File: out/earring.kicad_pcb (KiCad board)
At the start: 4 copper layers, 30.5 x 35.8 mm, 144 parts, among them J1 USB-C, Q1 ALS-PT19, Q2 CJ2101, Q3 BSS138W, Q4 CJ2101, Q5 BSS138W, SW1 BOOTSEL, SW2 PWR, U1 RP2350A, U2 LGS4056H, U3 NCP730-3.3, U4 TPS22913, U5 USBLC6-2P6, U6 LSM6DS3TR-C, U7 W25Q16JVUXIQ, Y1 12MHz

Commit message: One-button BOOTSEL, silicon D2/D3, button TVS, high-Vth latch FET
Folds the power-button simulation's findings into the board (user decisions
2026-10-24), each re-simulated, independently reviewed and re-reviewed.

- SW1 deleted. A long hold on the power button resets the chip into BOOTSEL
  (Q8/R26/R27, R28 680k + C75 timer, D5, U8 74LVC2G14GW, Q7 strap, C76/R29 ->
  Q6 RUN kick, C77). Fires 2.2-10.3 s typical, 2.0-19.4 s at U8's leakage
  limit. On battery the same hold turns the board off on release, which is
  the hardware force-off for hung firmware. Flash is never touched.
- Hot self-start fixed: D2 BAT54SW -> BAV99W, D3 B5819WS -> 1N4007WS. Board-off
  EN is now <= 0.03 V at 85 C (afabd86 reached 2.27 V). Cost: VSYS = VBUS - 0.8 V.
- Button ESD: D6 PESD5V0S1BL at the switch pad + R30 1k. A +-8 kV strike puts
  <= 22 mA into the latch (was ~24 A) and no longer counts as a press.
- Q4 CJ2101 -> LBSS84WT1G (VGS(th) 0.8-2.0 V): the latch's hot off-state
  margin no longer depends on an unspecified threshold tempco (review F2;
  design/sim/button/leakstudy.py).
- D4 BAV70W sourced from Nexperia (the Diodes part was down to 100 in stock).
- Testbench: netlist from circuit.py, afabd86 kept as a reference patch,
  54/54 runs pass, ESD/II-limit/pull-up/click-then-hold scenarios added.
- Placement: 14 new parts via scan_spot (12 back, Q6/R29 front in SW1's
  spot); DRC 0 errors, placed but NOT routed. Schematic regenerated
  (97 nets verified). Gates 1/2/6/8 updated with both reviews.

Firmware must change with this board: GPIO21 is active high with no pull-up,
and the long-press-off must be <= 1.5 s.

Co-Authored-By: Claude Opus 5.5 <noreply@anthropic.com>
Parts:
- removed SW1: BOOTSEL, earring:KEY-SMD_4P-L4.2-W3.2-P2.20-LS4.6
- added C75: 10u, earring:C_0603_1608Metric, B.Cu at (100.8, 93.2)
- added C76: 10n, earring:C_0402_1005Metric, B.Cu at (104.5, 90.8)
- added C77: 100n, earring:C_0402_1005Metric, B.Cu at (106.0, 93.0)
- added D5: 1N4148WS, earring:D_SOD-323, B.Cu at (100.8, 90.8)
- added D6: PESD5V0S1BL, earring:D_SOD-882, B.Cu at (94.0, 88.2)
- added Q6: BSS138W, earring:SOT-323_MOSFET, F.Cu at (99.0, 89.0)
- added Q7: BSS138W, earring:SOT-323_MOSFET, B.Cu at (107.2, 95.2)
- added Q8: CJ2101, earring:SOT-323_MOSFET, B.Cu at (96.5, 93.2)
- added R26: 100k, earring:R_0402_1005Metric, B.Cu at (97.2, 91.5)
- added R27: 4.7k, earring:R_0402_1005Metric, B.Cu at (95.2, 91.5)
- added R28: 680k, earring:R_0402_1005Metric, B.Cu at (99.0, 93.8)
- added R29: 1M, earring:R_0402_1005Metric, F.Cu at (96.8, 87.2)
- added R30: 1k, earring:R_0402_1005Metric, B.Cu at (94.5, 90.0)
- added U8: 74LVC2G14, earring:SOT-363_SC-70-6, B.Cu at (103.5, 93.0)
- D2: value BAT54S -> BAV99W
- D3: value B5819WS -> 1N4007WS
- Q4: value CJ2101 -> LBSS84WT1G
- moved C27 3.34 mm to (93.2, 91.5), turned to 0 degrees
- moved C17 0.11 mm to (107.3, 101.9)
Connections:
- D4 pad 1: BTN_SENSE -> PRESS_N
- SW2 pad 2: BTN_N -> BTN_EXT
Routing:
- net VBUS: track 3.81 -> 6.24 mm

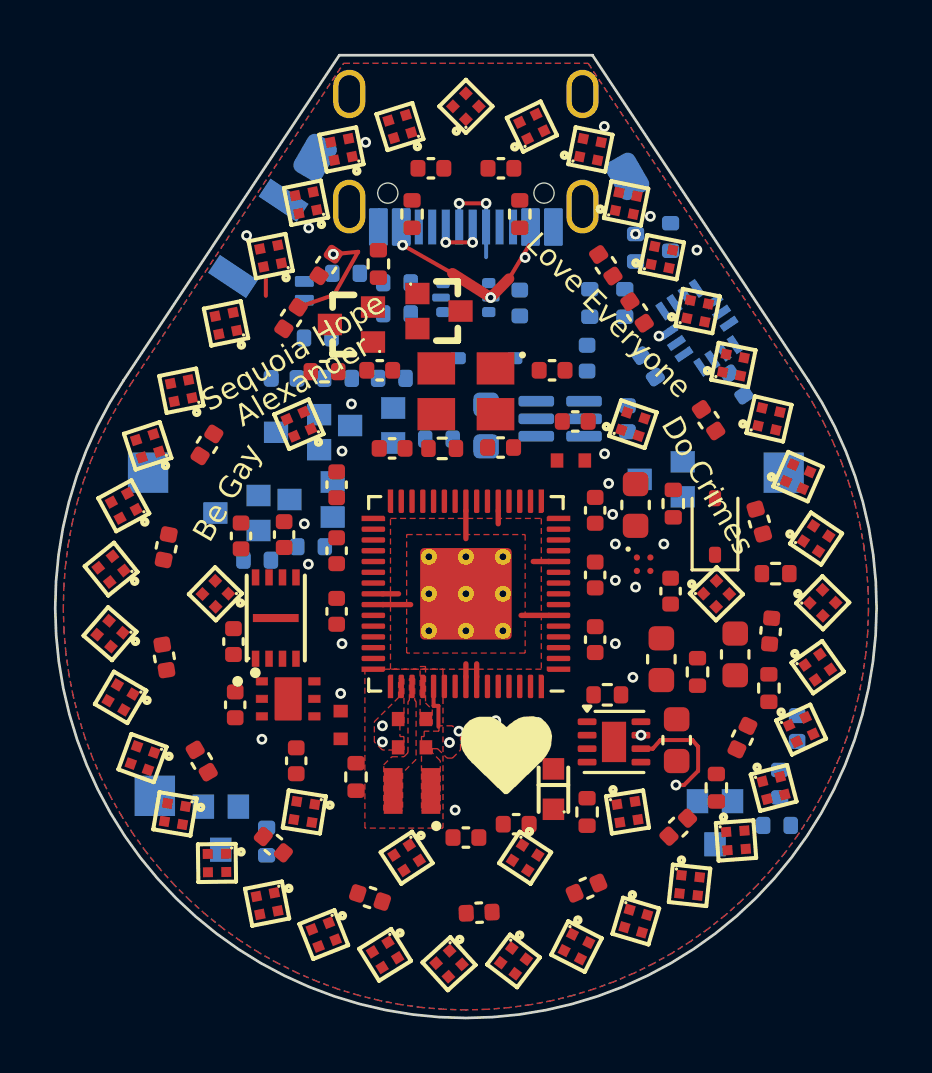
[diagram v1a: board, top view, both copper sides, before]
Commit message: LED ring: WS2816C-1313 (16-bit) in three switched zones; lock policy
User decisions 2026-10-24: switch the ring to WS2816C-1313/4P and split it
into left / right / centre zones. Independently reviewed (gates 1, 2, 6 pass).

- LEDs: SK6805-EC10 -> WS2816C-1313/4P (C42417612). 16-bit per channel plus
  gamma for the low-brightness range; VDD floor 3.3 V; idle 0.7-1.0 mA per LED;
  rated to 65 C; MSL 5a. New LED_WS2816C-1313 footprint (EasyEDA land, pin map
  checked against the datasheet: 1 VDD, 2 DO, 3 GND, 4 DI).
- Three zones, each its own chain, TPS22913 load switch (U4/U9/U10) and
  open-drain shifter pulled up to its own rail (Q3/Q9/Q10 + R23/R31/R32), so a
  dark zone draws nothing and can't be back-fed through its data line.
  Left LED1-18, right LED37->19 (reversed, enters at the tip), centre
  LED38-45. Data GPIO16/17/18 (adjacent: one PIO program), enables GPIO1/0/22.
- In2: VLED_C inner band, VLED_L / VLED_R split of the outer band, 3V3 disc.
- Placement: same ring centres, per-zone orientation; D3/C29 moved for
  LED44; zone drivers via scan_spot. DRC 0 errors, placed but NOT routed:
  the user routes it with their own GPU autorouter. route.py's SK6805-era
  freerouting workaround pre-routes are removed.
- Locked for the router: all LEDs, J1, SW2 (user request), plus BT1, Q1, and
  every part that locked copper or a fixed pour lands on (U1, U2, U5, R14,
  VREG cluster L1/C11/C12/C13/R13/C22). Everything else may be nudged.
- Schematic regenerated per zone (103 nets verified).

Firmware: three 48-bit chains (reset >= 280 us), data pins inverted and idle
high, power zones off rather than blanking them, keep a hard brightness cap.

Co-Authored-By: Claude Opus 5.5 <noreply@anthropic.com>
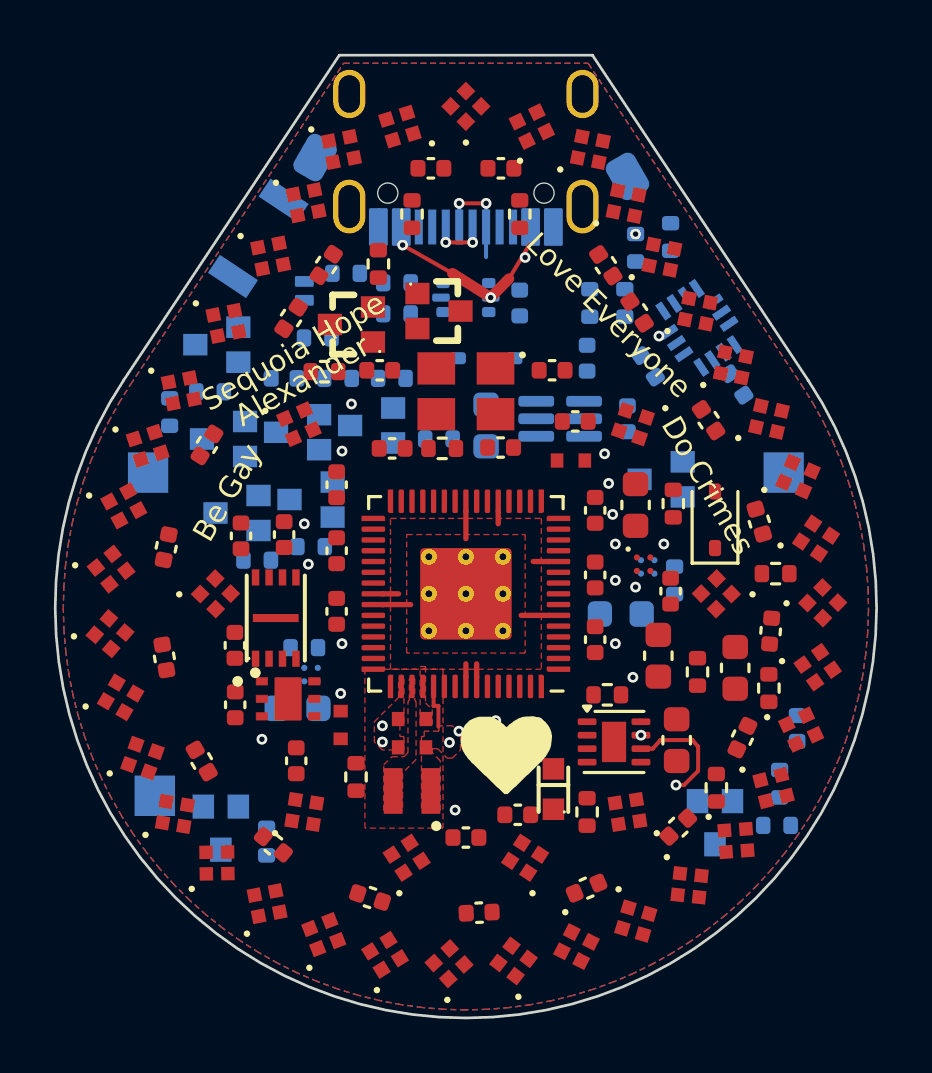
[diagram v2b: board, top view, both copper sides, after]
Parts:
- added C78: 10u, earring:C_0603_1608Metric, B.Cu at (105.8, 100.2)
- added C79: 10u, earring:C_0603_1608Metric, B.Cu at (93.8, 103.8)
- added Q10: BSS138W, earring:SOT-323_MOSFET, B.Cu at (91.0, 93.8)
- added Q9: BSS138W, earring:SOT-323_MOSFET, B.Cu at (90.8, 90.2)
- added R31: 1k, earring:R_0402_1005Metric, B.Cu at (90.5, 92.0)
- added R32: 1k, earring:R_0402_1005Metric, B.Cu at (89.0, 92.8)
- added R33: 10k, earring:R_0402_1005Metric, B.Cu at (107.8, 99.0)
- added R34: 10k, earring:R_0402_1005Metric, B.Cu at (94.0, 101.5)
- added U10: TPS22913, earring:YZV0004ADAD, B.Cu at (94.2, 102.5)
- added U9: TPS22913, earring:YZV0004ADAD, B.Cu at (106.8, 98.5)
- LED1, LED10, LED11, LED12, LED13, LED14, LED15, LED16, LED17, LED18, LED19, LED2, LED20, LED21, LED22, LED23, LED24, LED25, LED26, LED27, LED28, LED29, LED3, LED30, LED31, LED32, LED33, LED34, LED35, LED36, LED37, LED38, LED39, LED4, LED40, LED41, LED42, LED43, LED44, LED45, LED5, LED6, LED7, LED8, LED9: value SK6805-EC10 -> WS2816C-1313; footprint earring:LED_SK6805-EC10 -> earring:LED_WS2816C-1313
- moved C29 0.50 mm to (110.0, 102.2)
- moved C26 0.36 mm to (101.9, 107.7)
- moved D3 0.25 mm to (109.2, 96.8)
- moved C17 0.17 mm to (107.1, 101.8)
- moved C18 0.15 mm to (91.4, 101.4)
- turned LED1 to 11.4366 degrees
- turned LED10 to 59.6219 degrees
- turned LED11 to 70.003 degrees
- turned LED12 to 80.3842 degrees
- turned LED13 to 90.7653 degrees
- turned LED14 to 101.146 degrees
- turned LED15 to 111.528 degrees
- turned LED16 to 121.909 degrees
- turned LED17 to 132.29 degrees
- turned LED18 to 142.671 degrees
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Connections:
- net LED_D19 renamed LEDR_D18
- net LED_D20 renamed LEDR_D17
- net LED_D21 renamed LEDR_D16
- net LED_D22 renamed LEDR_D15
- net LED_D23 renamed LEDR_D14
- net LED_D24 renamed LEDR_D13
- net LED_D25 renamed LEDR_D12
- net LED_D26 renamed LEDR_D11
- net LED_D27 renamed LEDR_D10
- net LED_D28 renamed LEDR_D9
- net LED_D29 renamed LEDR_D8
- net LED_D30 renamed LEDR_D7
- net LED_D31 renamed LEDR_D6
- net LED_D32 renamed LEDR_D5
- net LED_D33 renamed LEDR_D4
- net LED_D34 renamed LEDR_D3
- net LED_D35 renamed LEDR_D2
- net LED_D36 renamed LEDR_D1
- net LED_DATA renamed LED_DATA_L
- net LED_EN renamed LED_EN_L
- C20 pad 1: VLED -> VLED_L
- C30 pad 1: VLED -> VLED_L
- C32 pad 1: VLED -> VLED_L
- C34 pad 1: VLED -> VLED_L
- C36 pad 1: VLED -> VLED_L
- C38 pad 1: VLED -> VLED_L
- C40 pad 1: VLED -> VLED_L
- C42 pad 1: VLED -> VLED_L
- C44 pad 1: VLED -> VLED_L
- C46 pad 1: VLED -> VLED_L
- C48 pad 1: VLED -> VLED_R
- C50 pad 1: VLED -> VLED_R
- C52 pad 1: VLED -> VLED_R
- C54 pad 1: VLED -> VLED_R
- C56 pad 1: VLED -> VLED_R
- C58 pad 1: VLED -> VLED_R
- C60 pad 1: VLED -> VLED_R
- C62 pad 1: VLED -> VLED_R
- C64 pad 1: VLED -> VLED_R
- C66 pad 1: VLED -> VLED_R
- C68 pad 1: VLED -> VLED_C
- C70 pad 1: VLED -> VLED_C
- C72 pad 1: VLED -> VLED_C
- C74 pad 1: VLED -> VLED_C
- LED1 pad 1: GND -> VLED_L
- LED1 pad 2: LED_D0 -> LEDL_D1
- LED1 pad 3: VLED -> GND
- LED1 pad 4: LED_D1 -> LEDL_D0
- LED10 pad 1: GND -> VLED_L
- LED10 pad 2: LED_D9 -> LEDL_D10
- LED10 pad 3: VLED -> GND
- LED10 pad 4: LED_D10 -> LEDL_D9
- LED11 pad 1: GND -> VLED_L
- LED11 pad 2: LED_D10 -> LEDL_D11
- LED11 pad 3: VLED -> GND
- LED11 pad 4: LED_D11 -> LEDL_D10
- LED12 pad 1: GND -> VLED_L
- LED12 pad 2: LED_D11 -> LEDL_D12
- LED12 pad 3: VLED -> GND
- LED12 pad 4: LED_D12 -> LEDL_D11
- LED13 pad 1: GND -> VLED_L
- LED13 pad 2: LED_D12 -> LEDL_D13
- LED13 pad 3: VLED -> GND
- LED13 pad 4: LED_D13 -> LEDL_D12
- LED14 pad 1: GND -> VLED_L
- LED14 pad 2: LED_D13 -> LEDL_D14
- LED14 pad 3: VLED -> GND
- LED14 pad 4: LED_D14 -> LEDL_D13
- LED15 pad 1: GND -> VLED_L
- LED15 pad 2: LED_D14 -> LEDL_D15
- LED15 pad 3: VLED -> GND
- LED15 pad 4: LED_D15 -> LEDL_D14
- LED16 pad 1: GND -> VLED_L
- LED16 pad 2: LED_D15 -> LEDL_D16
- LED16 pad 3: VLED -> GND
- LED16 pad 4: LED_D16 -> LEDL_D15
- LED17 pad 1: GND -> VLED_L
- LED17 pad 2: LED_D16 -> LEDL_D17
- LED17 pad 3: VLED -> GND
- LED17 pad 4: LED_D17 -> LEDL_D16
- LED18 pad 1: GND -> VLED_L
- LED18 pad 2: LED_D17 -> (no net)
- LED18 pad 3: VLED -> GND
- LED18 pad 4: LED_D18 -> LEDL_D17
- LED19 pad 1: GND -> VLED_R
- LED19 pad 2: LED_D18 -> (no net)
- LED19 pad 3: VLED -> GND
- LED2 pad 1: GND -> VLED_L
- LED2 pad 2: LED_D1 -> LEDL_D2
- LED2 pad 3: VLED -> GND
- LED2 pad 4: LED_D2 -> LEDL_D1
- LED20 pad 1: GND -> VLED_R
- LED20 pad 3: VLED -> GND
- LED21 pad 1: GND -> VLED_R
- LED21 pad 3: VLED -> GND
- LED22 pad 1: GND -> VLED_R
- LED22 pad 3: VLED -> GND
- LED23 pad 1: GND -> VLED_R
- LED23 pad 3: VLED -> GND
- LED24 pad 1: GND -> VLED_R
- LED24 pad 3: VLED -> GND
- LED25 pad 1: GND -> VLED_R
- LED25 pad 3: VLED -> GND
- LED26 pad 1: GND -> VLED_R
- LED26 pad 3: VLED -> GND
- LED27 pad 1: GND -> VLED_R
- LED27 pad 3: VLED -> GND
- LED28 pad 1: GND -> VLED_R
- LED28 pad 3: VLED -> GND
- LED29 pad 1: GND -> VLED_R
- LED29 pad 3: VLED -> GND
- LED3 pad 1: GND -> VLED_L
- LED3 pad 2: LED_D2 -> LEDL_D3
- LED3 pad 3: VLED -> GND
- LED3 pad 4: LED_D3 -> LEDL_D2
- LED30 pad 1: GND -> VLED_R
- LED30 pad 3: VLED -> GND
- LED31 pad 1: GND -> VLED_R
- LED31 pad 3: VLED -> GND
- LED32 pad 1: GND -> VLED_R
- LED32 pad 3: VLED -> GND
- LED33 pad 1: GND -> VLED_R
- LED33 pad 3: VLED -> GND
- LED34 pad 1: GND -> VLED_R
- LED34 pad 3: VLED -> GND
- LED35 pad 1: GND -> VLED_R
- LED35 pad 3: VLED -> GND
- LED36 pad 1: GND -> VLED_R
- LED36 pad 3: VLED -> GND
- LED37 pad 1: GND -> VLED_R
- LED37 pad 3: VLED -> GND
- LED37 pad 4: LED_D37 -> LEDR_D0
- LED38 pad 1: GND -> VLED_C
- LED38 pad 2: LED_D37 -> LEDC_D1
- LED38 pad 3: VLED -> GND
- LED38 pad 4: LED_D38 -> LEDC_D0
- LED39 pad 1: GND -> VLED_C
- LED39 pad 2: LED_D38 -> LEDC_D2
- LED39 pad 3: VLED -> GND
- LED39 pad 4: LED_D39 -> LEDC_D1
- LED4 pad 1: GND -> VLED_L
- LED4 pad 2: LED_D3 -> LEDL_D4
- LED4 pad 3: VLED -> GND
- LED4 pad 4: LED_D4 -> LEDL_D3
- LED40 pad 1: GND -> VLED_C
- LED40 pad 2: LED_D39 -> LEDC_D3
- LED40 pad 3: VLED -> GND
- LED40 pad 4: LED_D40 -> LEDC_D2
- LED41 pad 1: GND -> VLED_C
- LED41 pad 2: LED_D40 -> LEDC_D4
- LED41 pad 3: VLED -> GND
- LED41 pad 4: LED_D41 -> LEDC_D3
- LED42 pad 1: GND -> VLED_C
- LED42 pad 2: LED_D41 -> LEDC_D5
- LED42 pad 3: VLED -> GND
- LED42 pad 4: LED_D42 -> LEDC_D4
- LED43 pad 1: GND -> VLED_C
- LED43 pad 2: LED_D42 -> LEDC_D6
- LED43 pad 3: VLED -> GND
- LED43 pad 4: LED_D43 -> LEDC_D5
- LED44 pad 1: GND -> VLED_C
- LED44 pad 2: LED_D43 -> LEDC_D7
- LED44 pad 3: VLED -> GND
- LED44 pad 4: LED_D44 -> LEDC_D6
- LED45 pad 1: GND -> VLED_C
- LED45 pad 2: LED_D44 -> (no net)
- LED45 pad 3: VLED -> GND
- LED45 pad 4: (no net) -> LEDC_D7
- LED5 pad 1: GND -> VLED_L
- LED5 pad 2: LED_D4 -> LEDL_D5
- LED5 pad 3: VLED -> GND
- LED5 pad 4: LED_D5 -> LEDL_D4
- LED6 pad 1: GND -> VLED_L
- LED6 pad 2: LED_D5 -> LEDL_D6
- LED6 pad 3: VLED -> GND
- LED6 pad 4: LED_D6 -> LEDL_D5
- LED7 pad 1: GND -> VLED_L
- LED7 pad 2: LED_D6 -> LEDL_D7
- LED7 pad 3: VLED -> GND
- LED7 pad 4: LED_D7 -> LEDL_D6
- LED8 pad 1: GND -> VLED_L
- LED8 pad 2: LED_D7 -> LEDL_D8
- LED8 pad 3: VLED -> GND
- LED8 pad 4: LED_D8 -> LEDL_D7
- LED9 pad 1: GND -> VLED_L
- LED9 pad 2: LED_D8 -> LEDL_D9
- LED9 pad 3: VLED -> GND
- LED9 pad 4: LED_D9 -> LEDL_D8
- Q3 pad 3: LED_D0 -> LEDL_D0
- R23 pad 1: VLED -> VLED_L
- R23 pad 2: LED_D0 -> LEDL_D0
- U1 pad 2: (no net) -> LED_EN_R
- U1 pad 27: (no net) -> LED_DATA_C
- U1 pad 28: (no net) -> LED_DATA_R
- U1 pad 34: (no net) -> LED_EN_C
- U4 pad A1: VLED -> VLED_L
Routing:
- net VLED: track 4.17 -> 0.00 mm, vias 7 -> 0
- net LED_D3: track 0.62 -> 0.00 mm
- added copper zone on In2.Cu, net VLED_C
- added copper zone on In2.Cu, net VLED_L
- added copper zone on In2.Cu, net VLED_R
- removed copper zone on In2.Cu, net VLED

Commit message: Move 19 parts to the back to clear the area around the CPU
Flash U7/C25/R3, charger U2/C16/C17/R8, LDO U3/C18/C19, power path
D3/C29/R21/R22, VBUS tap R19/R20 and LED_L switch U4/C20/R10 now sit on
the back under the cell. All are <= 1.1 mm (datasheet max), the under-cell
cap for the 1.5 mm foam tape. Front courtyard area within r < 10 mm drops
from 107 to 57 mm^2; the back under U1 stays clear for escape vias.

route.py drops the freerouting assists anchored to the old front spots
(QSPI, CHRG/CHRG_DONE + U2 landing loop, LED_EN_L, U3 3V3 via); U2 is no
longer locked. gen_lipo_fit_svg.py gains heights for the new packages and
now fails instead of treating an unknown height as 0 mm.

DRC 0 errors (unrouted, 274 unconnected), cell fit clean, gate-6 review
PASS after fixes (design/gates/phase6.md).

Co-Authored-By: Claude Opus 5.5 <noreply@anthropic.com>
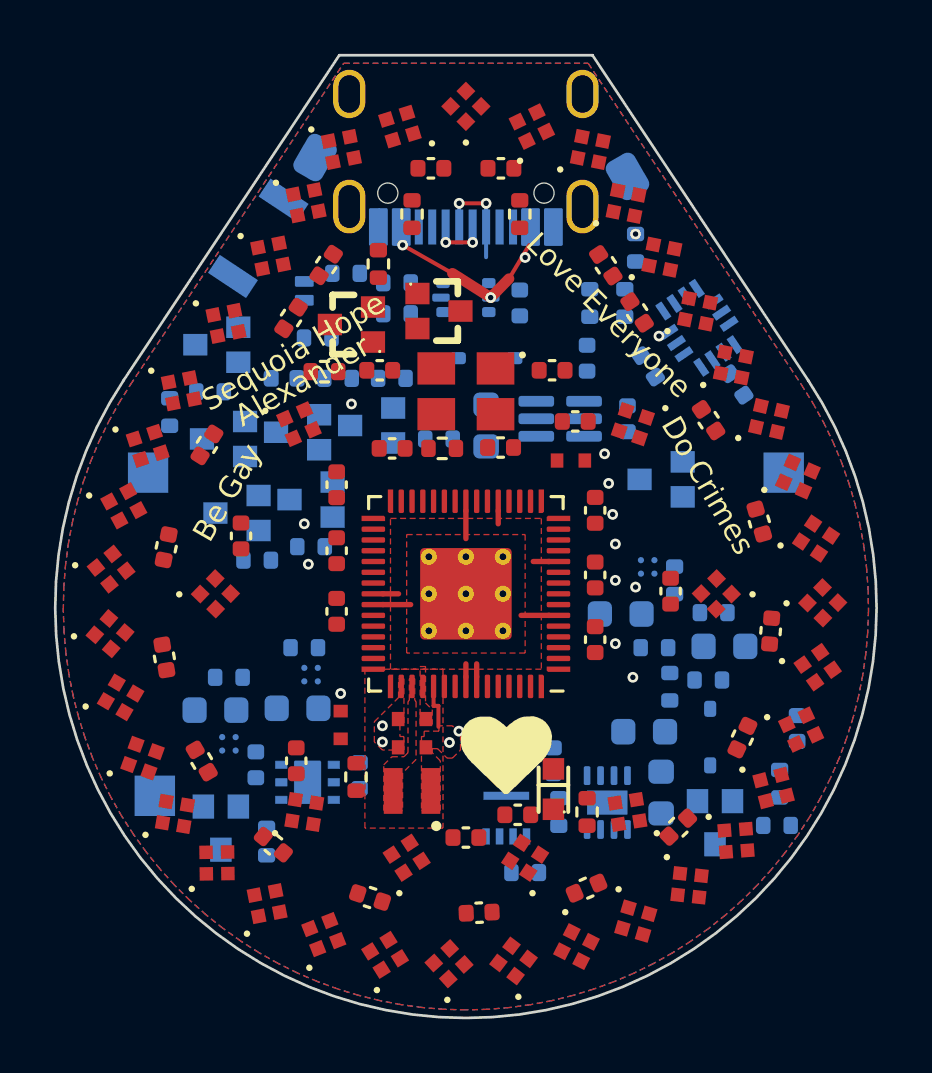
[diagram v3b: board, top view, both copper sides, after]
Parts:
- C16, C17, C18, C19, C20, C25, C29, D3, R19, R20, R21, R22, R3, R8, U2, U3, U4, U7: moved to B.Cu
- moved R10 23.2 mm to (91.2, 102.6), turned to 180 degrees
- moved C20 17.4 mm to (90.7, 103.8), turned to 0 degrees
- moved U4 16.8 mm to (91.2, 105.1)
- moved R3 14.8 mm to (102.2, 109.8), turned to 0 degrees
- moved C25 13.1 mm to (103.2, 105.7), turned to -90 degrees
- moved U7 10.8 mm to (101.5, 107.0), turned to 180 degrees
- moved D3 8.07 mm to (109.1, 104.8)
- moved R8 7.32 mm to (103.5, 107.6), turned to -90 degrees
- moved C19 5.31 mm to (96.0, 106.2), turned to -90 degrees
- moved C17 5.08 mm to (107.2, 106.9)
- moved C18 4.50 mm to (92.2, 105.8), turned to -90 degrees
- moved R22 4.01 mm to (109.0, 102.7), turned to 180 degrees
- moved R21 3.68 mm to (107.6, 103.0)
- moved U3 3.18 mm to (94.1, 106.5), turned to 180 degrees
- moved R20 2.72 mm to (109.2, 100.2)
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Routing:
- net CHRG_DONE: track 4.32 -> 0.00 mm, vias 2 -> 0
- net QSPI_SD3: vias 1 -> 0
- net QSPI_SD2: vias 1 -> 0
- net QSPI_SD1: vias 1 -> 0
- net QSPI_SD0: vias 1 -> 0
- net QSPI_SCLK: vias 1 -> 0
- net LED_EN_L: vias 1 -> 0
- net CHRG: vias 2 -> 0
- net 3V3: vias 8 -> 7
